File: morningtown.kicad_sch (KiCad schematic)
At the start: 11 parts, among them SW1 Test, U1 Pico, U2 DS3231M

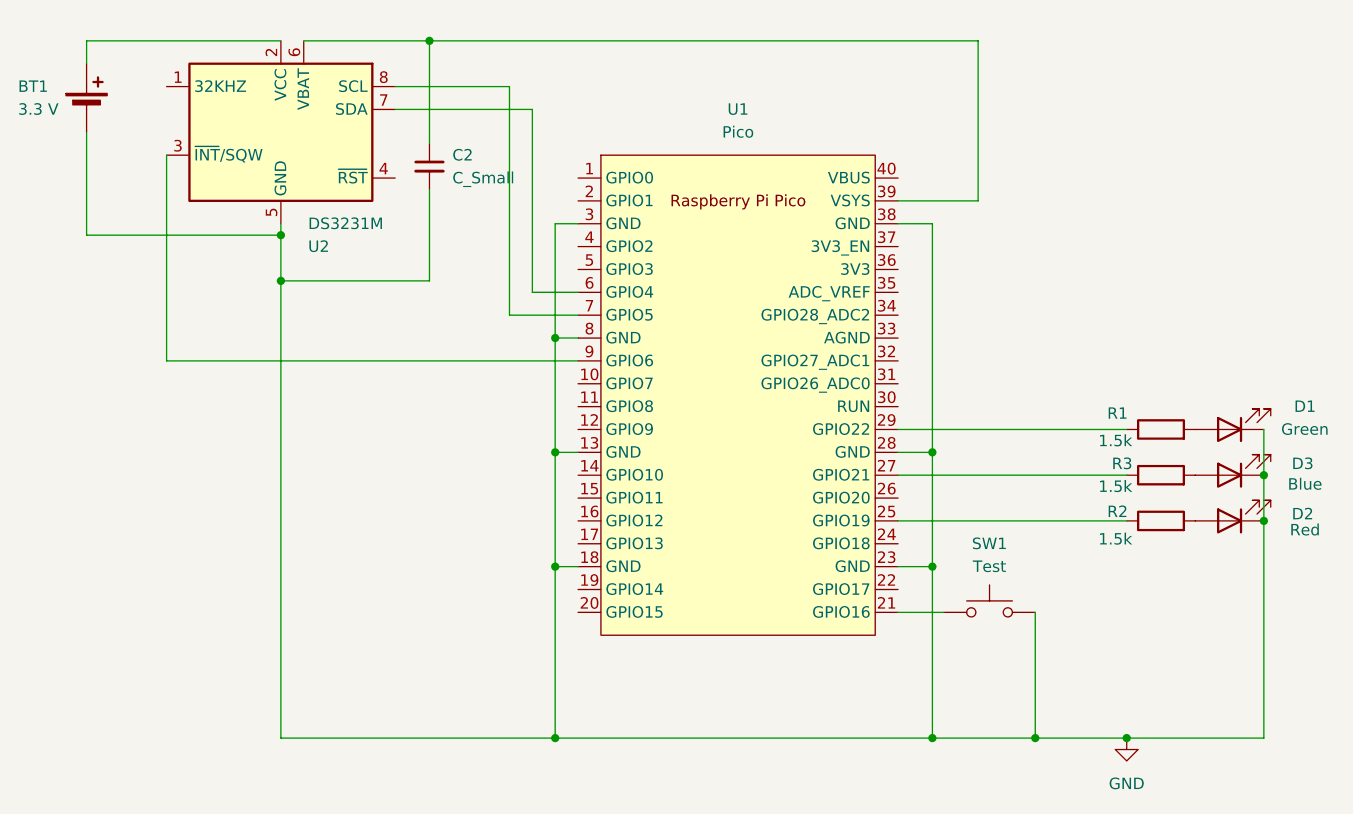
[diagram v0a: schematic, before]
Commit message: Fix r1.0 errata
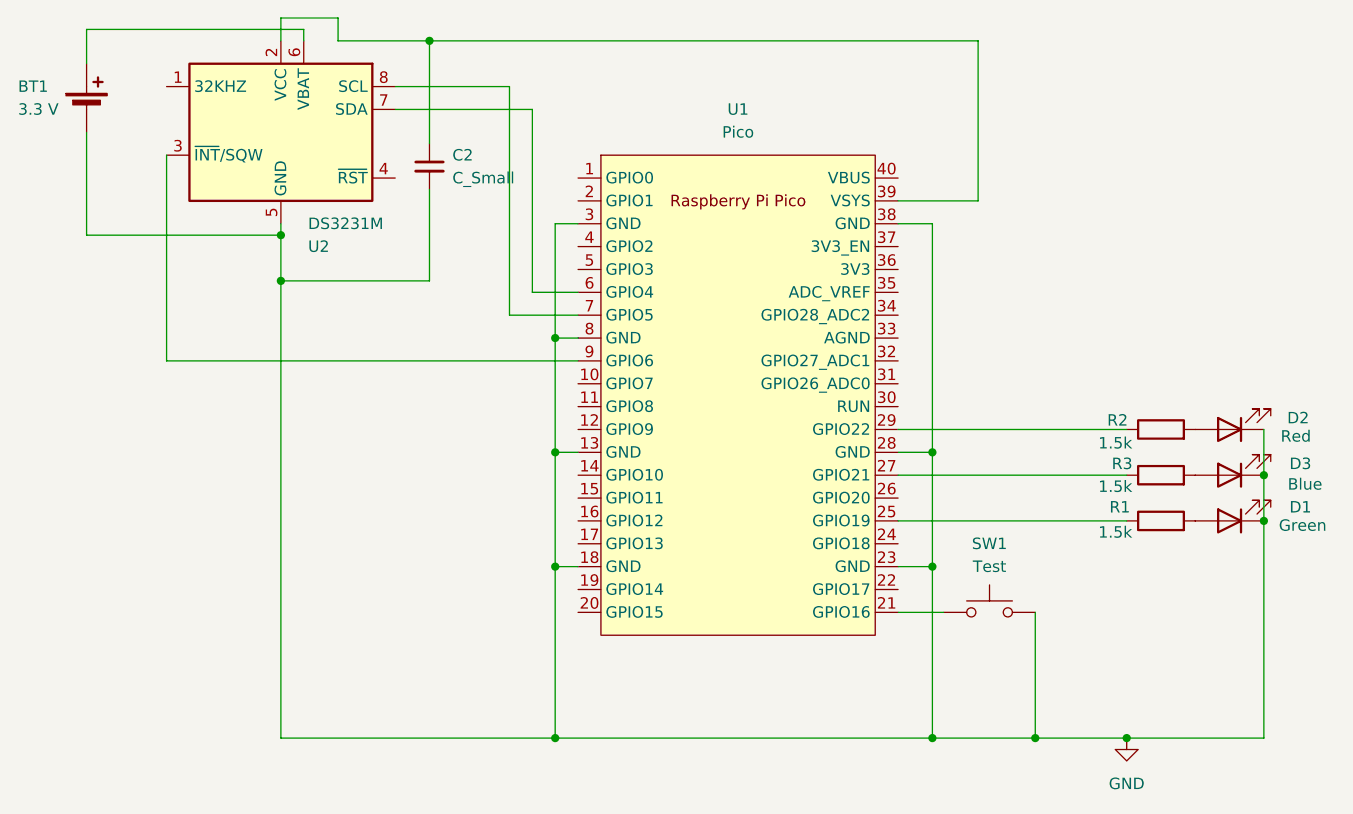
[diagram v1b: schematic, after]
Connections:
- net at U1.25 (GPIO19): now also R1.1; no longer R2.1
- net at U1.29 (GPIO22): now also R2.1; no longer R1.1
- net at C2.1, U1.39 (VSYS): now also U2.2 (VCC); no longer U2.6 (VBAT)
- net at BT1.1 (+): now also U2.6 (VBAT); no longer U2.2 (VCC)
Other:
- moved on the sheet: D1, D2, R1, R2

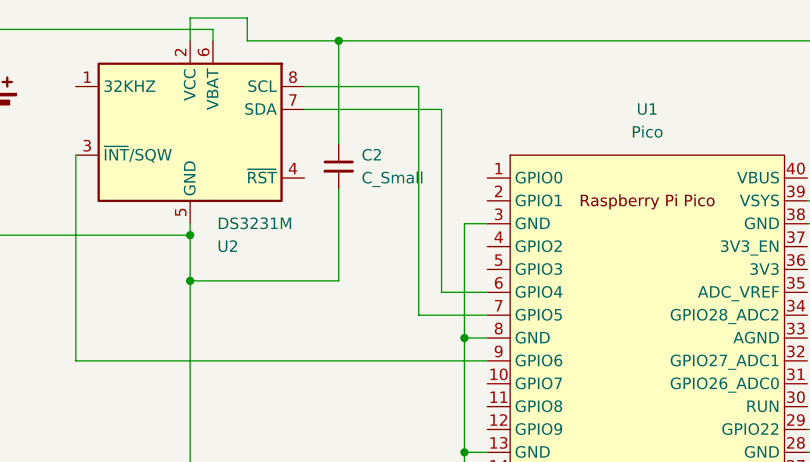
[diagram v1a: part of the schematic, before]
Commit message: Switch to SMD resistors and capacitors
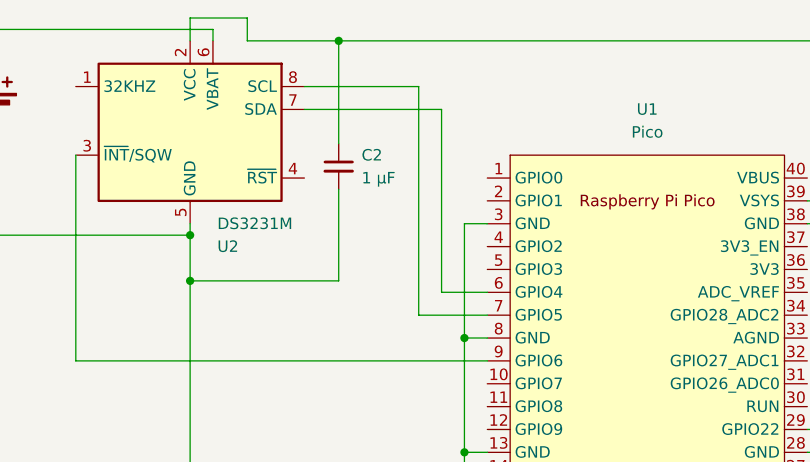
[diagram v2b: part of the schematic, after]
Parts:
- C2: value C_Small -> 1 µF; footprint Capacitor_THT:C_Disc_D3.0mm_W2.0mm_P2.50mm -> Capacitor_SMD:C_0805_2012Metric_Pad1.18x1.45mm_HandSolder
- R1, R2, R3: footprint Resistor_THT:R_Axial_DIN0207_L6.3mm_D2.5mm_P10.16mm_Horizontal -> Resistor_SMD:R_0805_2012Metric_Pad1.20x1.40mm_HandSolder
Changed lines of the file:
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@@
 			)
 		)
-		(property "Footprint" "Resistor_THT:R_Axial_DIN0207_L6.3mm_D2.5mm_P10.16mm_Horizontal"
+		(property "Footprint" "Resistor_SMD:R_0805_2012Metric_Pad1.20x1.40mm_HandSolder"
 			(at 147.32 108.458 90)
 			(effects
@@
 			)
 		)
-		(property "Footprint" "Resistor_THT:R_Axial_DIN0207_L6.3mm_D2.5mm_P10.16mm_Horizontal"
+		(property "Footprint" "Resistor_SMD:R_0805_2012Metric_Pad1.20x1.40mm_HandSolder"
 			(at 147.32 113.538 90)
 			(effects
@@
 			)
 		)
-		(property "Footprint" "Resistor_THT:R_Axial_DIN0207_L6.3mm_D2.5mm_P10.16mm_Horizontal"
+		(property "Footprint" "Resistor_SMD:R_0805_2012Metric_Pad1.20x1.40mm_HandSolder"
 			(at 147.32 103.378 90)
 			(effects
@@
 			)
 		)
-		(property "Value" "C_Small"
+		(property "Value" "1 µF"
 			(at 68.58 73.6662 0)
 			(effects
@@
 			)
 		)
-		(property "Footprint" "Capacitor_THT:C_Disc_D3.0mm_W2.0mm_P2.50mm"
+		(property "Footprint" "Capacitor_SMD:C_0805_2012Metric_Pad1.18x1.45mm_HandSolder"
 			(at 66.04 72.39 0)
 			(effects
